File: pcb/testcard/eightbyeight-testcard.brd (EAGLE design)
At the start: 60 x 60 mm, 28 parts

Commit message: Update test card to fit new test jig
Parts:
- moved DIGITAL_TEST 10.4 mm to (4.00, 23.0), flipped to the top
- moved ARM_BOOT 10.0 mm to (39.7, 16.2)
- moved LED_CLK 10.0 mm to (37.7, 16.2)
- moved LED_DATA 10.0 mm to (33.7, 16.2)
- moved LED_OE 10.0 mm to (35.7, 16.2)
- moved LED_STB 10.0 mm to (35.7, 14.2), flipped to the bottom
- moved +3V3 10.0 mm to (47.0, 57.0)
- moved 5V 10.0 mm to (29.6, 54.5)
- moved ARM_3V3 10.0 mm to (42.0, 6.50)
- moved ARM_RESET 10.0 mm to (48.0, 6.50)
- moved ARM_RX 10.0 mm to (44.0, 6.50)
- moved ARM_TCK 10.0 mm to (44.0, 4.50)
- moved ARM_TMS 10.0 mm to (42.0, 4.50)
- moved ARM_TX 10.0 mm to (46.0, 6.50)
- moved BOOST_5V 10.0 mm to (18.8, 8.50)
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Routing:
- net GND: track 3.06 -> 82.3 mm, vias 0 -> 8
- net ARM_3V3: track 125.9 -> 87.7 mm
- net LED_STB: track 21.3 -> 58.1 mm, vias 0 -> 1
- net LED_CLK: track 24.1 -> 51.1 mm, vias 0 -> 1
- net ARM_RX: track 14.2 -> 39.6 mm, vias 1 -> 0
- net +5V: track 13.7 -> 35.0 mm
- net ARM_RX1: track 32.9 -> 53.8 mm
- net LED_OE: track 21.5 -> 42.1 mm, vias 1 -> 0
- net +3V3: track 34.7 -> 55.0 mm, vias 1 -> 0
- net ARM_BOOTLOADER: track 32.3 -> 46.8 mm, vias 0 -> 1
- net ESP_GPIO0: track 31.7 -> 43.7 mm
- net I2C_SDA: track 39.7 -> 50.3 mm, vias 0 -> 1
- net BUTTON: track 65.2 -> 57.2 mm, vias 2 -> 1
- net ARM_RESET: track 18.7 -> 25.3 mm, vias 1 -> 0
- net I2C_SCL: track 47.9 -> 53.7 mm, vias 0 -> 1
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- added copper zone on layer 1, net GND
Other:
- board size 60 x 60 mm -> 70 x 60 mm
- board text added: "EightByEight Test Card RevB 2016-07 Blinkinlabs, LLC"
- board text removed: "EightByEight Test Card RevA 2016-07 Blinkinlabs, LLC"

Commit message: Update test card with proper sized holes
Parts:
- +3V3, ESP_GPIO16, ESP_GPIO5, GND: value TEST_POINT -> TEST_POINT2.55MM; device DevicesToMerge:IO_HOLE_1.4MM -> DevicesToMerge:IO_HOLE_2.55MM
- 5V, ARM_3V3, ARM_BOOT, ARM_RESET, ARM_RX, ARM_RX1, ARM_TCK, ARM_TMS, ARM_TX, BOOST_5V, BUTTON, ESP_GPIO0, ESP_RESET, GND_, I2C_SCL, I2C_SDA, LED_CLK, LED_DATA, LED_OE, LED_STB, VBAT: value TEST_POINT -> TEST_POINT1.4MM
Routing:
- net GND: track 82.3 -> 126.5 mm, vias 8 -> 2
- net ARM_RX: track 39.6 -> 19.0 mm, vias 0 -> 2
- net ARM_RESET: track 25.3 -> 43.8 mm
- net +3V3: track 55.0 -> 69.8 mm
- net LED_STB: track 58.1 -> 45.8 mm, vias 1 -> 0
- net ARM_3V3: track 87.7 -> 76.8 mm, vias 1 -> 2
- net ARM_BOOTLOADER: track 46.8 -> 56.1 mm
- net ARM_TX: track 24.6 -> 20.9 mm, vias 1 -> 2
- net LED_CLK: track 51.1 -> 54.6 mm, vias 1 -> 0
- net I2C_SDA: track 50.3 -> 46.8 mm
- net VBAT: track 102.6 -> 99.5 mm, vias 0 -> 1
- net ESP_GPIO16: track 75.7 -> 73.3 mm, vias 1 -> 0
- net BUTTON: track 57.2 -> 56.0 mm, vias 1 -> 0
- net +5V: track 35.0 -> 36.0 mm
- net BOOST_5V: track 59.0 -> 58.5 mm, vias 0 -> 1
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
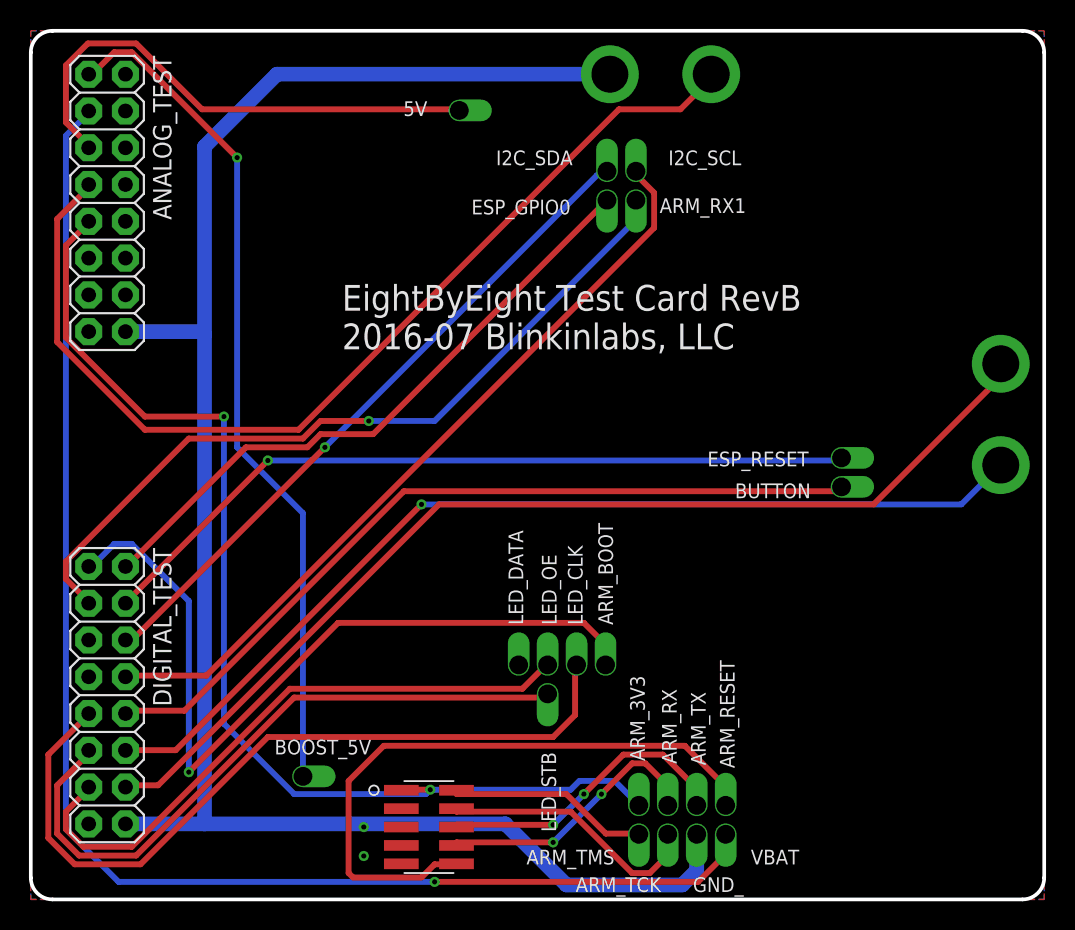
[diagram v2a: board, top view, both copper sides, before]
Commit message: Update testcard to fit current test jig
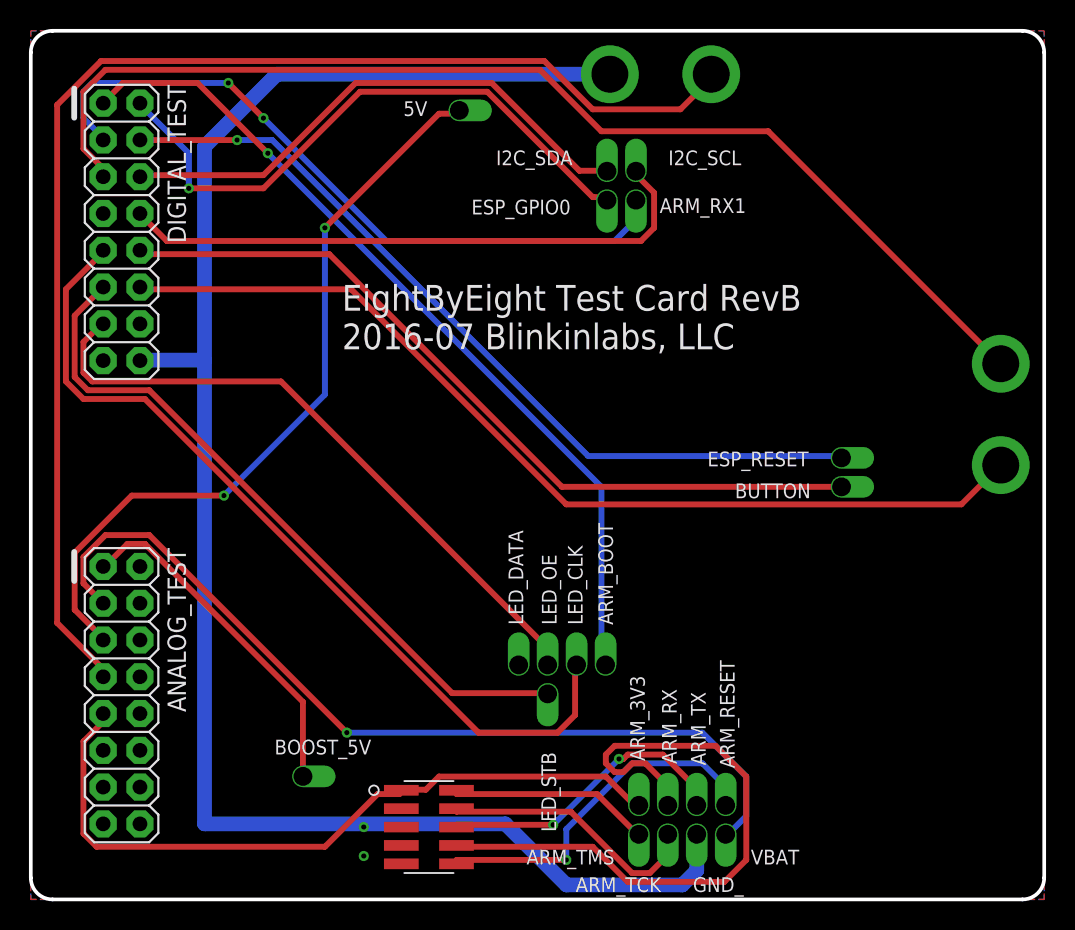
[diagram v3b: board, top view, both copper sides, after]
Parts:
- moved ANALOG_TEST 34.0 mm to (5.00, 23.0)
- moved DIGITAL_TEST 32.0 mm to (5.00, 55.0)
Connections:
- net ESP_GPIO16: now also DIGITAL_TEST.5; no longer DIGITAL_TEST.14
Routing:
- net VBAT: track 99.5 -> 61.7 mm
- net BOOST_5V: track 58.5 -> 24.1 mm, vias 1 -> 0
- net ARM_RX: track 19.0 -> 45.7 mm, vias 2 -> 0
- net ARM_3V3: track 76.8 -> 50.6 mm, vias 2 -> 0
- net +3V3: track 69.8 -> 89.8 mm
- net ARM_RESET: track 43.8 -> 24.8 mm, vias 0 -> 1
- net +5V: track 36.0 -> 52.8 mm, vias 0 -> 2
- net I2C_SCL: track 53.8 -> 41.1 mm
- net I2C_SDA: track 46.8 -> 37.5 mm, vias 1 -> 0
- net GND: track 126.5 -> 120.0 mm
- net ESP_GPIO16: track 73.3 -> 78.8 mm
- net ARM_RX1: track 54.1 -> 48.8 mm, vias 1 -> 2
- net LED_CLK: track 54.6 -> 59.3 mm
- net ESP_RESET: track 53.6 -> 57.5 mm
- net LED_STB: track 45.8 -> 48.7 mm
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
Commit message: Update test card pcb notes
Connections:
- removed net LED_DATA: DIGITAL_TEST.7
- net LED_DAT_0: now also DIGITAL_TEST.7
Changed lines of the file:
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@@
 <signal name="LED_DAT_0">
 <contactref element="LED_DATA" pad="P$1"/>
+<contactref element="DIGITAL_TEST" pad="7"/>
+<wire x1="5" y1="47.38" x2="33.7" y2="16.2" width="0" layer="19" extent="1-1"/>
 </signal>
 <signal name="LED_OE">
@@
 <via x="16.3728" y="51.544" extent="1-16" drill="0.35"/>
 </signal>
-<signal name="LED_DATA">
-<contactref element="DIGITAL_TEST" pad="7"/>
-</signal>
 <signal name="ESP_GPIO5">
